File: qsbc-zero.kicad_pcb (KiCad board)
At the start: 4 copper layers, 80 x 80 mm, 242 parts, among them J1 Micro_SD_Card_Det1, J10 Conn_02x18_Odd_Even, J11 Conn_01x09_Male, J2 USB4105, J3 USB-A-S-F-B-VU, J4 USB4105, J5 Conn_02x18_Odd_Even, J6 J1B1211CCD, J7 Conn_01x06_Male, J8 Conn_01x09_Male, J9 Conn_01x02_Male, SW1 SW_Push, U1 MX6UL-VM, U11 TPD4EUSB30, U12 74LVC1G04, U13 D5V0H1B2LP, U14 D5V0H1B2LP, U18 DP83825, U2 MC32PF1510A6EP, U25 TPD4EUSB30, U26 TPD4EUSB30, U27 TPD4EUSB30, U3 MT41K256M16, U4 TUSB320, U5 AP22811B, U6 TPD4EUSB30, U7 D5V0H1B2LP, U8 D5V0H1B2LP, U9 W25Q512JVEIQ, Y1 24Mhz, Y2 32.768kHz

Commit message: misc rev2 fixes
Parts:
- added C97: 0.1uF, Capacitor_SMD:C_0402_1005Metric, F.Cu at (184.6, 134.9)
- C81: footprint Capacitor_SMD:C_0402_1005Metric -> Capacitor_SMD:C_0201_0603Metric
- C82: value 100uF -> 10uF; footprint Capacitor_Tantalum_SMD:CP_EIA-3528-15_AVX-H -> Capacitor_SMD:C_0402_1005Metric
- C93: footprint Capacitor_Tantalum_SMD:CP_EIA-3528-15_AVX-H -> Capacitor_SMD:CP_Elec_6.3x4.9
- moved C82 11.1 mm to (184.6, 133.8), turned to 180 degrees
- moved C69 4.48 mm to (190.5, 129.7), turned to -90 degrees
- moved D2 4.00 mm to (207.4, 67.9)
- moved R129 4.00 mm to (207.4, 71.6)
- moved D1 4.00 mm to (203.4, 67.9)
- moved R128 4.00 mm to (203.4, 71.6)
- moved C94 3.11 mm to (172.8, 134.0)
- moved U13 2.72 mm to (174.1, 134.8)
- moved C95 2.66 mm to (191.1, 121.2)
- moved R39 2.66 mm to (192.8, 121.0)
- moved R40 2.66 mm to (192.8, 122.1)
- moved U12 2.66 mm to (192.4, 124.7)
- moved R43 2.34 mm to (166.0, 135.7)
- moved C93 2.11 mm to (170.8, 139.6)
- moved R41 2.10 mm to (167.0, 135.7)
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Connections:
- C82 pad 1: VSYS_5V -> /USB/VBUS_1
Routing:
- net Net-(R40-Pad1): track 15.0 -> 8.05 mm
- net /Peripherals/LED_0: track 46.0 -> 50.7 mm
- net /Peripherals/LED_1: track 50.8 -> 46.9 mm
- net GND: track 288.5 -> 285.2 mm, vias 191 -> 188
- net Net-(J4-PadA5): track 11.1 -> 8.76 mm
- net /USB/VBUS_1: track 9.74 -> 11.9 mm
- net Net-(J4-PadB5): track 6.57 -> 8.59 mm
- net VSYS_5V: track 169.2 -> 167.8 mm
- net USB1_ID: track 17.4 -> 16.1 mm
- net I2C4_SCL: track 64.1 -> 63.2 mm
- net I2C4_SDA: track 64.1 -> 63.2 mm
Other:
- board text added: "QSBC-ZERO Rev 2.0 gitlab.com/quentin-z80/qsbc-zero"
- board text removed: "QSBC-ZERO Rev 1.0 gitlab.com/quentin-z80/qsbc-zero"

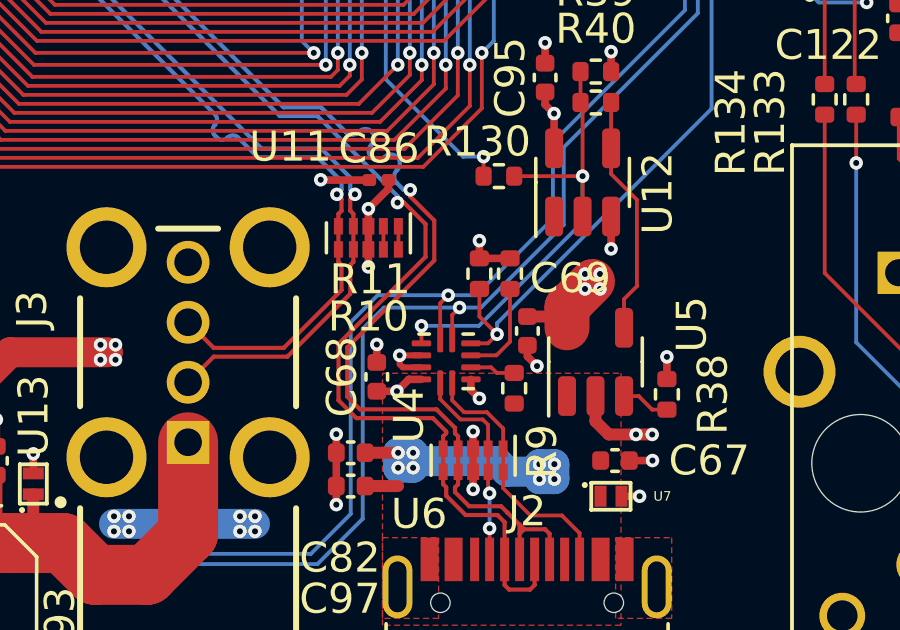
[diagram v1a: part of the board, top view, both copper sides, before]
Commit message: tusb320: fix swaped SDA/SCL
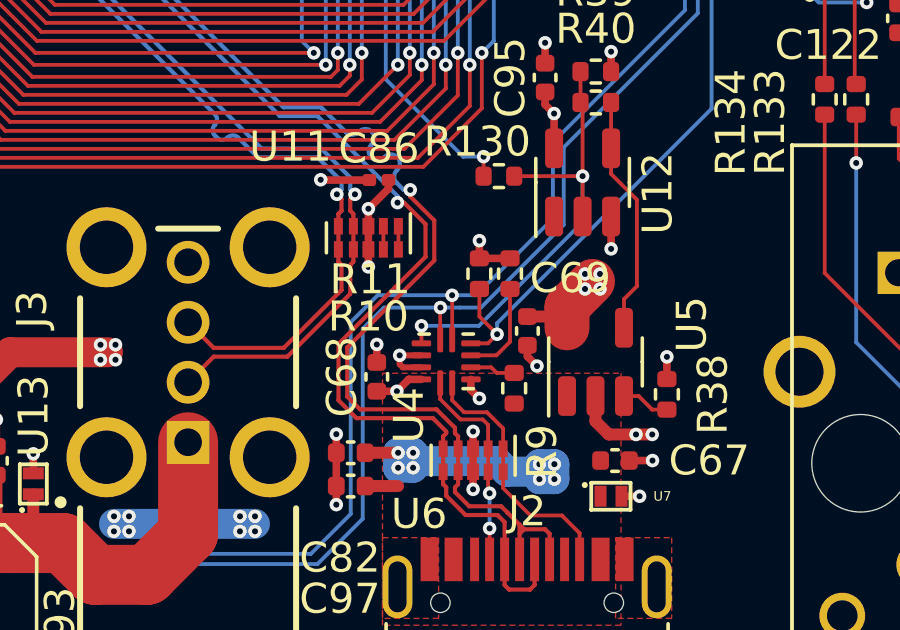
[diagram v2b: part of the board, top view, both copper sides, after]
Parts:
- C93: value 100uF -> 120uF
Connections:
- U4 pad 7: I2C4_SCL -> I2C4_SDA
- U4 pad 8: I2C4_SDA -> I2C4_SCL
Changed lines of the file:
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@@
     (property "DigiKey_PN" "490-13409-1-ND")
     (property "MPN" "GCM155C71A105KE38D")
-    (property "Rating" "6.3V/20%")
+    (property "Rating" "10V/20%")
     (property "Sheetfile" "power.kicad_sch")
     (property "Sheetname" "Power")
@@
     (property "DigiKey_PN" "490-13409-1-ND")
     (property "MPN" "GCM155C71A105KE38D")
-    (property "Rating" "6.3V/20%")
+    (property "Rating" "10V/20%")
     (property "Sheetfile" "power.kicad_sch")
     (property "Sheetname" "Power")
@@
       (net 192 "~{USB1_INT}") (pinfunction "~{INT}/OUT3") (pintype "open_collector"))
     (pad "7" smd roundrect locked (at 0.725 0.2 90) (size 0.85 0.2) (layers "F.Cu" "F.Paste" "F.Mask") (roundrect_rratio 0.25)
-      (net 215 "I2C4_SCL") (pinfunction "SDA/OUT1") (pintype "bidirectional"))
+      (net 214 "I2C4_SDA") (pinfunction "SDA/OUT1") (pintype "bidirectional"))
     (pad "8" smd roundrect locked (at 0.725 -0.2 90) (size 0.85 0.2) (layers "F.Cu" "F.Paste" "F.Mask") (roundrect_rratio 0.25)
-      (net 214 "I2C4_SDA") (pinfunction "SCL/OUT2") (pintype "bidirectional"))
+      (net 215 "I2C4_SCL") (pinfunction "SCL/OUT2") (pintype "bidirectional"))
     (pad "9" smd roundrect locked (at 0.6 -0.825 90) (size 0.2 0.65) (layers "F.Cu" "F.Paste" "F.Mask") (roundrect_rratio 0.25)
       (net 193 "USB1_ID") (pinfunction "ID") (pintype "open_collector"))
@@
     (property "DigiKey_PN" "490-13409-1-ND")
     (property "MPN" "GCM155C71A105KE38D")
-    (property "Rating" "6.3V/20%")
+    (property "Rating" "10V/20%")
     (property "Sheetfile" "power.kicad_sch")
     (property "Sheetname" "Power")
@@
     (descr "Capacitor SMD 0402 (1005 Metric), square (rectangular) end terminal, IPC_7351 nominal, (Body size source: IPC-SM-782 page 76, https://www.pcb-3d.com/wordpress/wp-content/uploads/ipc-sm-782a_amendment_1_and_2.pdf), generated with kicad-footprint-generator")
     (tags "capacitor")
-    (property "DigiKey_PN" "1276-1469-1-ND")
-    (property "MPN" "CL05A225MQ5NNNC")
+    (property "DigiKey_PN" "1276-1467-1-ND")
+    (property "MPN" "CL05A225MP5NSNC")
     (property "Rating" "10V/20%")
     (property "Sheetfile" "power.kicad_sch")
@@
     (descr "SMD capacitor, aluminum electrolytic, Panasonic C5, 6.3x4.9mm")
     (tags "capacitor electrolytic")
-    (property "DigiKey_PN" "478-8198-1-ND")
-    (property "MPN" "F931A107MBA")
+    (property "DigiKey_PN" "732-6413-1-ND")
+    (property "MPN" "875105244013")
     (property "Rating" "10V/20%")
     (property "Sheetfile" "usb.kicad_sch")
@@
       (effects (font (size 1 1) (thickness 0.15)))
     )
-    (fp_text value "100uF" (at 0 4.35 90) (layer "F.Fab")
+    (fp_text value "120uF" (at 0 4.35 90) (layer "F.Fab")
       (effects (font (size 1 1) (thickness 0.15)))
     )
@@
     (property "DigiKey_PN" "490-13409-1-ND")
     (property "MPN" "GCM155C71A105KE38D")
-    (property "Rating" "6.3V/20%")
+    (property "Rating" "10V/20%")
     (property "Sheetfile" "power.kicad_sch")
     (property "Sheetname" "Power")
@@
     (property "DigiKey_PN" "490-13409-1-ND")
     (property "MPN" "GCM155C71A105KE38D")
-    (property "Rating" "6.3V/20%")
+    (property "Rating" "10V/20%")
     (property "Sheetfile" "power.kicad_sch")
     (property "Sheetname" "Power")
@@
     (property "DigiKey_PN" "490-13409-1-ND")
     (property "MPN" "GCM155C71A105KE38D")
-    (property "Rating" "6.3V/20%")
+    (property "Rating" "10V/20%")
     (property "Sheetfile" "power.kicad_sch")
     (property "Sheetname" "Power")
@@
     (property "DigiKey_PN" "490-13409-1-ND")
     (property "MPN" "GCM155C71A105KE38D")
-    (property "Rating" "6.3V/20%")
+    (property "Rating" "10V/20%")
     (property "Sheetfile" "power.kicad_sch")
     (property "Sheetname" "Power")
@@
   (segment (start 186.99 130.099999) (end 186.987312 130.102687) (width 0.127) (layer "F.Cu") (net 193))
   (segment (start 192.29 121.043953) (end 192.29 122.073953) (width 0.127) (layer "F.Cu") (net 193))
-  (segment (start 186.99 129.52) (end 186.99 130.099999) (width 0.127) (layer "F.Cu") (net 193))
   (segment (start 192.36 124.53) (end 192.36 122.143953) (width 0.127) (layer "F.Cu") (net 193))
+  (segment (start 192.36 122.143953) (end 192.29 122.073953) (width 0.127) (layer "F.Cu") (net 193))
+  (segment (start 186.99 129.52) (end 186.99 130.099999) (width 0.127) (layer "F.Cu") (net 193))
   (segment (start 192.36 125.875986) (end 192.36 124.53) (width 0.127) (layer "F.Cu") (net 193))
   (segment (start 192.36 124.53) (end 190.08 124.53) (width 0.127) (layer "F.Cu") (net 193))
-  (segment (start 192.36 122.143953) (end 192.29 122.073953) (width 0.127) (layer "F.Cu") (net 193))
   (via (at 186.99 129.52) (size 0.45) (drill 0.2) (layers "F.Cu" "B.Cu") (remove_unused_layers) (keep_end_layers) (net 193))
   (via (at 192.36 124.53) (size 0.45) (drill 0.2) (layers "F.Cu" "B.Cu") (net 193))
@@
   (segment (start 190.2 113.49) (end 190.51 113.8) (width 0.127) (layer "F.Cu") (net 206))
   (segment (start 195.773 108.96) (end 195.593 108.78) (width 0.127) (layer "F.Cu") (net 214))
-  (segment (start 187.612312 128.767688) (end 187.612312 129.977687) (width 0.127) (layer "F.Cu") (net 214))
   (segment (start 164.334574 127.89) (end 163.8375 127.89) (width 0.127) (layer "F.Cu") (net 214))
+  (segment (start 188.012312 128.502312) (end 188.01 128.5) (width 0.127) (layer "F.Cu") (net 214))
   (segment (start 195.593 108.78) (end 193.8 108.78) (width 0.127) (layer "F.Cu") (net 214))
   (segment (start 195.773 108.96) (end 196.82 108.96) (width 0.127) (layer "F.Cu") (net 214))
   (segment (start 165.718287 129.273713) (end 164.334574 127.89) (width 0.127) (layer "F.Cu") (net 214))
-  (segment (start 187.88 128.5) (end 187.612312 128.767688) (width 0.127) (layer "F.Cu") (net 214))
+  (segment (start 188.012312 129.977687) (end 188.012312 128.502312) (width 0.127) (layer "F.Cu") (net 214))
   (via (at 195.773 108.96) (size 0.45) (drill 0.2) (layers "F.Cu" "B.Cu") (remove_unused_layers) (keep_end_layers) (net 214))
+  (via (at 188.01 128.5) (size 0.45) (drill 0.2) (layers "F.Cu" "B.Cu") (net 214))
   (via (at 165.718287 129.273713) (size 0.45) (drill 0.2) (layers "F.Cu" "B.Cu") (remove_unused_layers) (keep_end_layers) (net 214))
-  (via (at 187.88 128.5) (size 0.45) (drill 0.2) (layers "F.Cu" "B.Cu") (remove_unused_layers) (keep_end_layers) (net 214))
   (segment (start 191.37 125.94) (end 188.81 128.5) (width 0.127) (layer "B.Cu") (net 214))
   (segment (start 185.53 128.5) (end 187.88 128.5) (width 0.127) (layer "B.Cu") (net 214))
@@
   (segment (start 183.3 137.12) (end 184.63 135.79) (width 0.127) (layer "B.Cu") (net 214))
   (segment (start 195.773 118.997) (end 191.37 123.4) (width 0.127) (layer "B.Cu") (net 214))
-  (segment (start 188.26 128.91) (end 188.012312 129.157688) (width 0.127) (layer "F.Cu") (net 215))
   (segment (start 194.02 111.39) (end 193.01 110.38) (width 0.127) (layer "F.Cu") (net 215))
   (segment (start 165.07 128.02) (end 164.54 127.49) (width 0.127) (layer "F.Cu") (net 215))
-  (segment (start 188.012312 129.157688) (end 188.012312 129.977687) (width 0.127) (layer "F.Cu") (net 215))
+  (segment (start 187.612312 128.917688) (end 187.62 128.91) (width 0.127) (layer "F.Cu") (net 215))
   (segment (start 196.2 111.39) (end 194.02 111.39) (width 0.127) (layer "F.Cu") (net 215))
   (segment (start 164.54 127.49) (end 163.8375 127.49) (width 0.127) (layer "F.Cu") (net 215))
   (segment (start 196.2 111.39) (end 196.82 111.39) (width 0.127) (layer "F.Cu") (net 215))
   (segment (start 193.01 110.38) (end 193 110.38) (width 0.127) (layer "F.Cu") (net 215))
+  (segment (start 187.612312 129.977687) (end 187.612312 128.917688) (width 0.127) (layer "F.Cu") (net 215))
   (via (at 196.2 111.39) (size 0.45) (drill 0.2) (layers "F.Cu" "B.Cu") (remove_unused_layers) (keep_end_layers) (net 215))
   (via (at 165.07 128.02) (size 0.45) (drill 0.2) (layers "F.Cu" "B.Cu") (remove_unused_layers) (keep_end_layers) (net 215))
-  (via (at 188.26 128.91) (size 0.45) (drill 0.2) (layers "F.Cu" "B.Cu") (remove_unused_layers) (keep_end_layers) (net 215))
+  (via (at 187.62 128.91) (size 0.45) (drill 0.2) (layers "F.Cu" "B.Cu") (net 215))
   (segment (start 191.73 123.57) (end 191.73 126.15) (width 0.127) (layer "B.Cu") (net 215))
   (segment (start 196.2 119.1) (end 191.73 123.57) (width 0.127) (layer "B.Cu") (net 215))

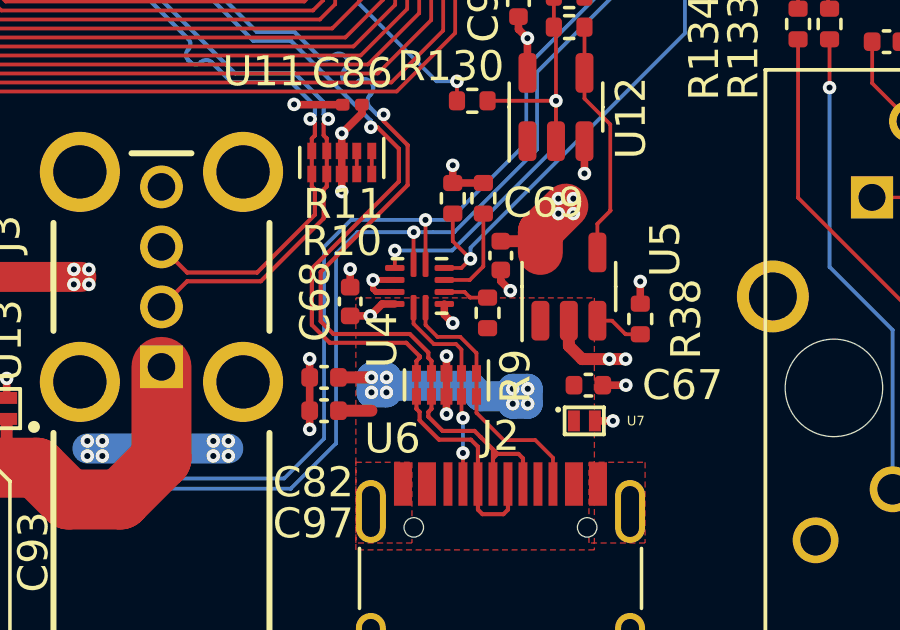
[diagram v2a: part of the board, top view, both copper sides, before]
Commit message: tusb320: use drp mode
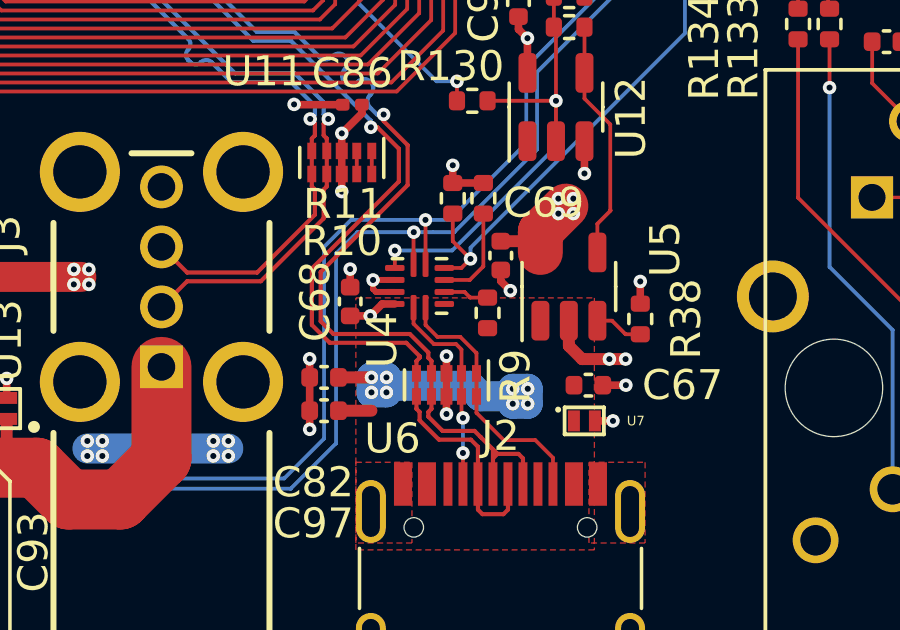
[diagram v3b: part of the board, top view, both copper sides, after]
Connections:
- U4 pad 3: GND -> unconnected-(U4-Pad3)
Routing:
- net GND: track 285.2 -> 284.5 mm, vias 188 -> 187
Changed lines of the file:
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@@
   (net 272 "I2C2_SCL")
   (net 273 "Net-(D3-Pad2)")
+  (net 274 "unconnected-(U4-Pad3)")
   (footprint "Resistor_SMD:R_0402_1005Metric" (layer "F.Cu")
     (at 201.12 112.65 -90)
@@
       (net 139 "/USB/CC2") (pinfunction "CC2") (pintype "bidirectional"))
     (pad "3" smd roundrect locked (at -0.6 0.825 90) (size 0.2 0.65) (layers "F.Cu" "F.Paste" "F.Mask") (roundrect_rratio 0.25)
-      (net 136 "GND") (pinfunction "PORT") (pintype "input"))
+      (net 274 "unconnected-(U4-Pad3)") (pinfunction "PORT") (pintype "input+no_connect"))
     (pad "4" smd roundrect locked (at -0.2 0.825 90) (size 0.2 0.65) (layers "F.Cu" "F.Paste" "F.Mask") (roundrect_rratio 0.25)
       (net 19 "Net-(R9-Pad2)") (pinfunction "VBUS_DET") (pintype "input"))
@@
   (segment (start 215.034876 81.074876) (end 215.04 81.08) (width 0.254) (layer "F.Cu") (net 136))
   (segment (start 195.57 67.34) (end 195.33 67.58) (width 0.4) (layer "F.Cu") (net 136))
-  (segment (start 188.637312 131.657312) (end 188.92 131.94) (width 0.254) (layer "F.Cu") (net 136))
   (segment (start 189.4 101.98) (end 189.8 102.38) (width 0.254) (layer "F.Cu") (net 136))
   (segment (start 189.26 102.64) (end 189.62 102.64) (width 0.254) (layer "F.Cu") (net 136))
@@
   (segment (start 174.42 94.61) (end 174.545 94.735) (width 0.254) (layer "F.Cu") (net 136))
   (segment (start 203.91 119.75) (end 202.89 119.75) (width 0.254) (layer "F.Cu") (net 136))
-  (segment (start 188.637312 131.302687) (end 188.637312 131.657312) (width 0.254) (layer "F.Cu") (net 136))
   (segment (start 185.3 105.88) (end 185 105.88) (width 0.254) (layer "F.Cu") (net 136))
   (segment (start 189.62 102.64) (end 189.8 102.82) (width 0.254) (layer "F.Cu") (net 136))
@@
   (via (at 161.611241 138.74) (size 0.45) (drill 0.2) (layers "F.Cu" "B.Cu") (remove_unused_layers) (keep_end_layers) (free) (net 136))
   (via (at 215.045124 111.085124) (size 0.45) (drill 0.2) (layers "F.Cu" "B.Cu") (remove_unused_layers) (keep_end_layers) (net 136))
-  (via (at 188.92 131.94) (size 0.45) (drill 0.2) (layers "F.Cu" "B.Cu") (remove_unused_layers) (keep_end_layers) (net 136))
   (via (at 180.7 96.54) (size 0.45) (drill 0.2) (layers "F.Cu" "B.Cu") (remove_unused_layers) (keep_end_layers) (net 136))
   (via (at 194.26 135.2) (size 0.45) (drill 0.2) (layers "F.Cu" "B.Cu") (remove_unused_layers) (keep_end_layers) (net 136))
